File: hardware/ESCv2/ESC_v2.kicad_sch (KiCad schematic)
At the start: 56 parts, among them J1 Conn_02x13_Odd_Even, J2 Conn_01x02, Q1 AON7544, Q2 AON7544, Q3 AON7544, Q4 AON7544, Q5 AON7544, Q6 AON7544, U1 MT6701CT, U2 DRV8305NPHPR

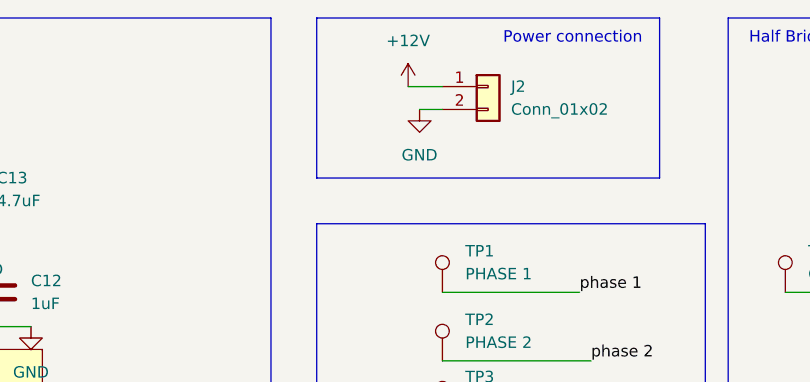
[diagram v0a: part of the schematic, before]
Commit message: improved Kelvin shunts
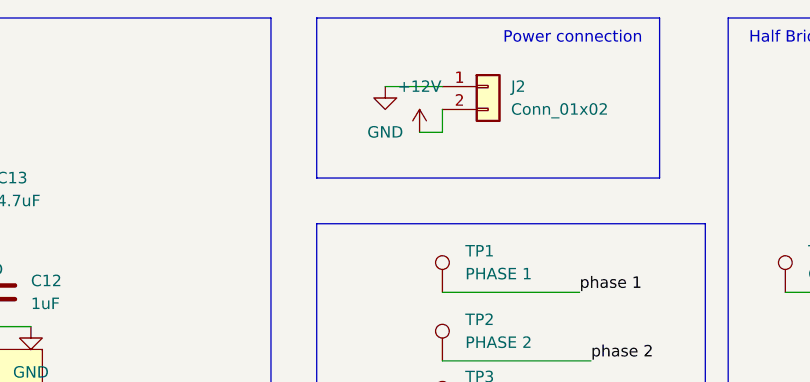
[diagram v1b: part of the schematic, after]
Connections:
- net +12V: now also J2.2 (Pin_2); no longer J2.1 (Pin_1)
- net GND: now also J2.1 (Pin_1); no longer J2.2 (Pin_2)
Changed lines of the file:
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@@
 	(wire
 		(pts
+			(xy 148.59 27.94) (xy 151.13 27.94)
+		)
+		(stroke
+			(width 0)
+			(type default)
+		)
+	)
+	(wire
+		(pts
 			(xy 27.94 176.53) (xy 27.94 173.99)
 		)
@@
 	(wire
 		(pts
+			(xy 144.78 22.86) (xy 151.13 22.86)
+		)
+		(stroke
+			(width 0)
+			(type default)
+		)
+	)
+	(wire
+		(pts
 			(xy 58.42 156.21) (xy 63.5 156.21)
 		)
@@
 	(wire
 		(pts
-			(xy 148.59 25.4) (xy 151.13 25.4)
-		)
-		(stroke
-			(width 0)
-			(type default)
-		)
-	)
-	(wire
-		(pts
 			(xy 27.94 191.77) (xy 39.37 191.77)
 		)
@@
 	(wire
 		(pts
+			(xy 151.13 27.94) (xy 151.13 25.4)
+		)
+		(stroke
+			(width 0)
+			(type default)
+		)
+	)
+	(wire
+		(pts
 			(xy 88.9 45.72) (xy 88.9 49.53)
 		)
@@
 	(wire
 		(pts
-			(xy 147.32 22.86) (xy 151.13 22.86)
-		)
-		(stroke
-			(width 0)
-			(type default)
-		)
-	)
-	(wire
-		(pts
 			(xy 229.87 77.47) (xy 229.87 80.01)
 		)
@@
 	(symbol
 		(lib_id "power:+12V")
-		(at 147.32 22.86 0)
+		(at 148.59 27.94 0)
 		(unit 1)
 		(body_style 1)
@@
 		(fields_autoplaced yes)
 		(property "Reference" "#PWR026"
-			(at 147.32 26.67 0)
+			(at 148.59 31.75 0)
 			(hide yes)
 			(show_name no)
@@
 		)
 		(property "Value" "+12V"
-			(at 147.32 17.78 0)
+			(at 148.59 22.86 0)
 			(show_name no)
 			(do_not_autoplace no)
@@
 		)
 		(property "Footprint" ""
-			(at 147.32 22.86 0)
+			(at 148.59 27.94 0)
 			(hide yes)
 			(show_name no)
@@
 		)
 		(property "Datasheet" ""
-			(at 147.32 22.86 0)
+			(at 148.59 27.94 0)
 			(hide yes)
 			(show_name no)
@@
 		)
 		(property "Description" "Power symbol creates a global label with name \"+12V\""
-			(at 147.32 22.86 0)
+			(at 148.59 27.94 0)
 			(hide yes)
 			(show_name no)
@@
 	(symbol
 		(lib_id "power:GND")
-		(at 148.59 25.4 0)
+		(at 144.78 22.86 0)
 		(unit 1)
 		(body_style 1)
@@
 		(fields_autoplaced yes)
 		(property "Reference" "#PWR027"
-			(at 148.59 31.75 0)
+			(at 144.78 29.21 0)
 			(hide yes)
 			(show_name no)
@@
 		)
 		(property "Value" "GND"
-			(at 148.59 30.48 0)
+			(at 144.78 27.94 0)
 			(show_name no)
 			(do_not_autoplace no)
@@
 		)
 		(property "Footprint" ""
-			(at 148.59 25.4 0)
+			(at 144.78 22.86 0)
 			(hide yes)
 			(show_name no)
@@
 		)
 		(property "Datasheet" ""
-			(at 148.59 25.4 0)
+			(at 144.78 22.86 0)
 			(hide yes)
 			(show_name no)
@@
 		)
 		(property "Description" "Power symbol creates a global label with name \"GND\" , ground"
-			(at 148.59 25.4 0)
+			(at 144.78 22.86 0)
 			(hide yes)
 			(show_name no)

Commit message: Improved kelvin shunts (for real this time), bootstrap caps closer to the DRV chip, added GND pour and a beautiful otter for good luck
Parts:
- added NT1, NT2, NT3: NetTie_2, NetTie:NetTie-2_SMD_Pad0.5mm, symbol Device:NetTie_2
- D1: LCSC ID C7461 -> C7461
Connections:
- net GND: now also NT1.2, NT2.2, NT3.2; no longer U2.20 (SP3), U2.22 (SP2), U2.24 (SP1)
- new net SP1: NT2.1, U2.24 (SP1)
- new net SP2: NT3.1, U2.22 (SP2)
- new net SP3: NT1.1, U2.20 (SP3)
